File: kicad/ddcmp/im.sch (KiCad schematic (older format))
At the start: 10 parts, among them J2 RX, J3 TX, U2 max3491ecpd

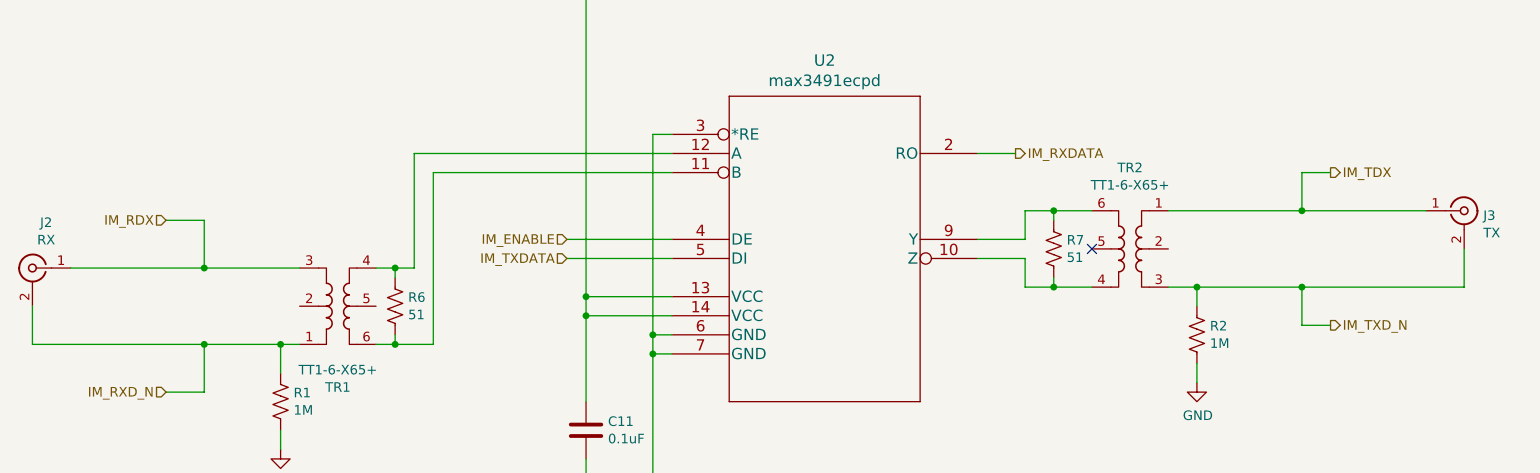
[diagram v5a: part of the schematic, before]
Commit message: Documentation improvements, small schematic fixes. Also firmware improvements, particularly clock rate accuracy.
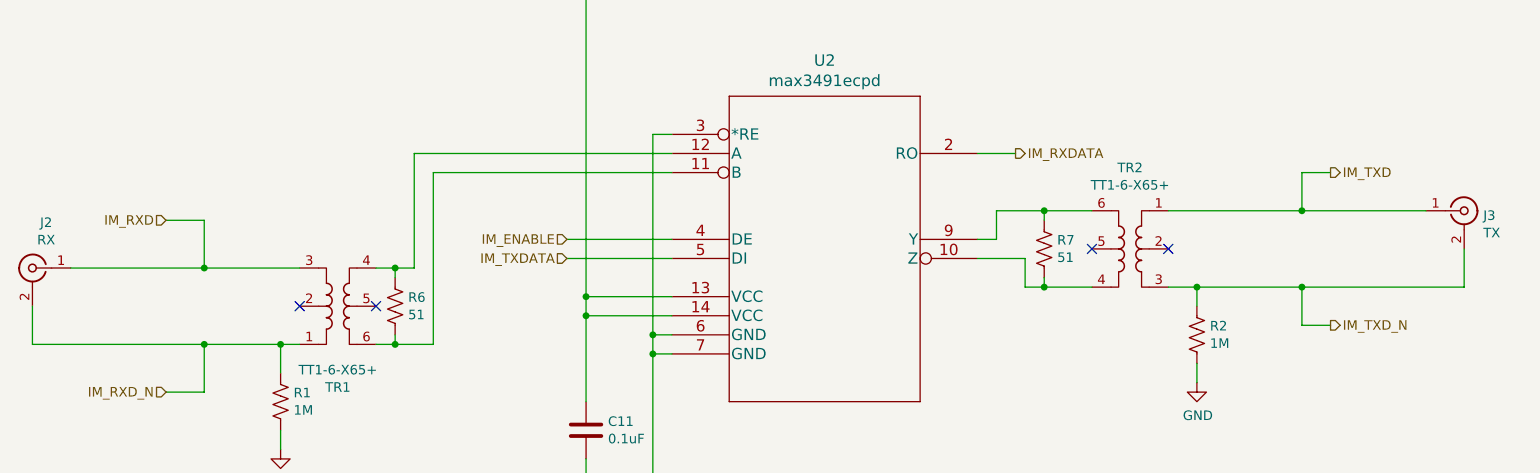
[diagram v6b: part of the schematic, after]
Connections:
- net IM_RDX renamed IM_RXD
- net IM_TDX renamed IM_TXD
- no-connect marks 1 -> 4
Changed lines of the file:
@@
 Wire Wire Line
 	6400 3000 6400 2850
-Wire Wire Line
-	6750 3000 6550 3000
-Wire Wire Line
-	6400 2600 6550 2600
-Wire Wire Line
-	6400 2750 6400 2600
-Wire Wire Line
-	6150 2750 6400 2750
 $Comp
 L ddcmp_symbols:max3491ecpd U?
@@
 Text HLabel 8000 3200 2    50   Output ~ 0
 IM_TXD_N
-Text HLabel 8000 2400 2    50   Output ~ 0
-IM_TDX
 Wire Wire Line
 	2100 2900 2100 2650
@@
 IM_RXD_N
 Text HLabel 1900 2650 0    50   Input ~ 0
-IM_RDX
+IM_RXD
 Wire Wire Line
 	4550 3150 4100 3150
@@
 Wire Wire Line
 	2800 1200 4100 1200
-$Comp
-L ddcmp_symbols:R_US R7
-U 1 1 60BD0969
-P 6550 2800
-F 0 "R7" H 6618 2846 50  0000 L CNN
-F 1 "51" H 6618 2755 50  0000 L CNN
-F 2 "ddcmp_parts:R_Axial_DIN0207_L6.3mm_D2.5mm_P10.16mm_Horizontal" V 6590 2790 50  0001 C CNN
-F 3 "https://www.yageo.com/upload/media/product/products/datasheet/lr/Yageo_LR_CFR_1.pdf" H 6550 2800 50  0001 C CNN
-F 4 "51QBK-ND" H 6550 2800 50  0001 C CNN "Digikey part"
-F 5 "Yageo" H 6550 2800 50  0001 C CNN "Vendor"
-F 6 "CFR-25JB-52-51R" H 6550 2800 50  0001 C CNN "Vendor part"
-	1    6550 2800
-	1    0    0    -1
-$EndComp
 $Comp
 L ddcmp_symbols:R_US R6
@@
 $EndComp
 Wire Wire Line
-	6550 2950 6550 3000
-Connection ~ 6550 3000
-Wire Wire Line
-	6550 3000 6400 3000
-Wire Wire Line
-	6550 2650 6550 2600
-Connection ~ 6550 2600
-Wire Wire Line
-	6550 2600 6750 2600
-Wire Wire Line
 	3100 2950 3100 2900
 Connection ~ 3100 2900
@@
 Wire Wire Line
 	3100 3300 3300 3300
+Text HLabel 8000 2400 2    50   Output ~ 0
+IM_TXD
+NoConn ~ 7150 2800
+NoConn ~ 3000 3100
+NoConn ~ 2600 3100
+Wire Wire Line
+	6400 3000 6500 3000
+Wire Wire Line
+	6250 2600 6250 2750
+Wire Wire Line
+	6250 2750 6150 2750
+Wire Wire Line
+	6250 2600 6500 2600
+$Comp
+L ddcmp_symbols:R_US R7
+U 1 1 60E4A38A
+P 6500 2800
+F 0 "R7" H 6568 2846 50  0000 L CNN
+F 1 "51" H 6568 2755 50  0000 L CNN
+F 2 "ddcmp_parts:R_Axial_DIN0207_L6.3mm_D2.5mm_P10.16mm_Horizontal" V 6540 2790 50  0001 C CNN
+F 3 "https://www.yageo.com/upload/media/product/products/datasheet/lr/Yageo_LR_CFR_1.pdf" H 6500 2800 50  0001 C CNN
+F 4 "51QBK-ND" H 6500 2800 50  0001 C CNN "Digikey part"
+F 5 "Yageo" H 6500 2800 50  0001 C CNN "Vendor"
+F 6 "CFR-25JB-52-51R" H 6500 2800 50  0001 C CNN "Vendor part"
+	1    6500 2800
+	1    0    0    -1
+$EndComp
+Wire Wire Line
+	6500 2600 6500 2650
+Connection ~ 6500 2600
+Wire Wire Line
+	6500 2600 6750 2600
+Wire Wire Line
+	6500 2950 6500 3000
+Connection ~ 6500 3000
+Wire Wire Line
+	6500 3000 6750 3000
 $EndSCHEMATC
